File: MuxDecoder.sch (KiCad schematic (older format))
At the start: 2 parts, among them U3 4001, U4 4071

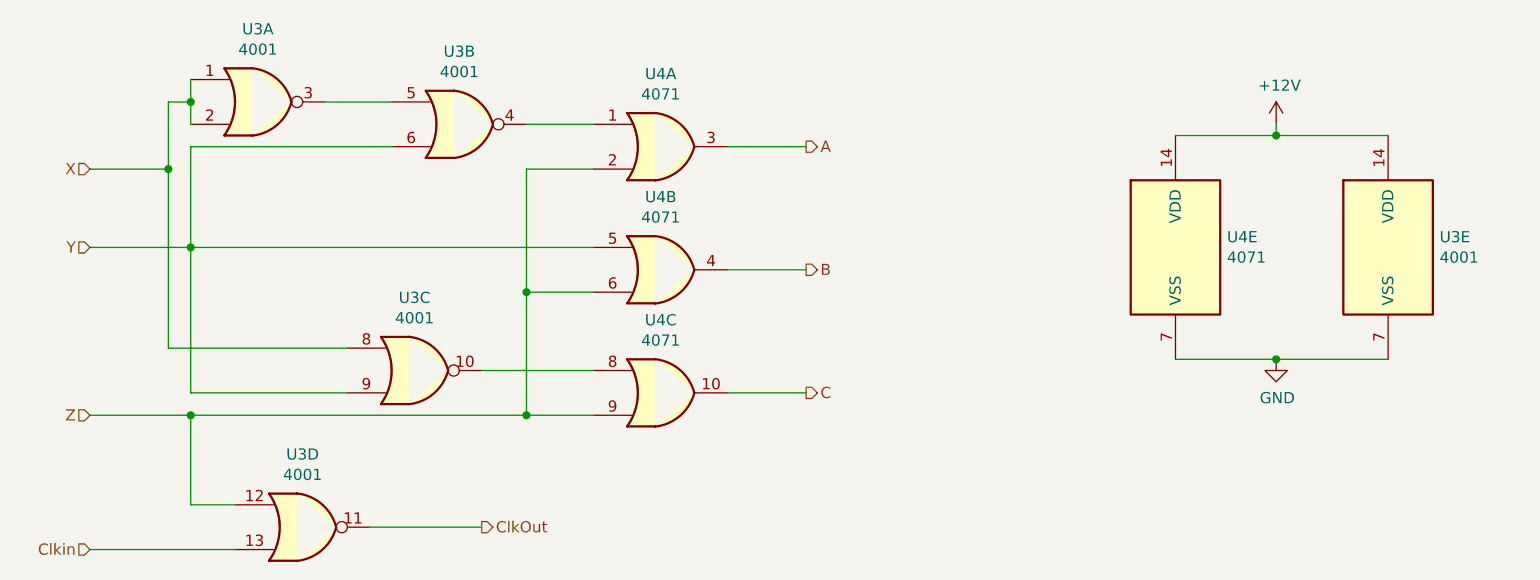
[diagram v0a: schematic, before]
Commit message: Renamed: NTE4001
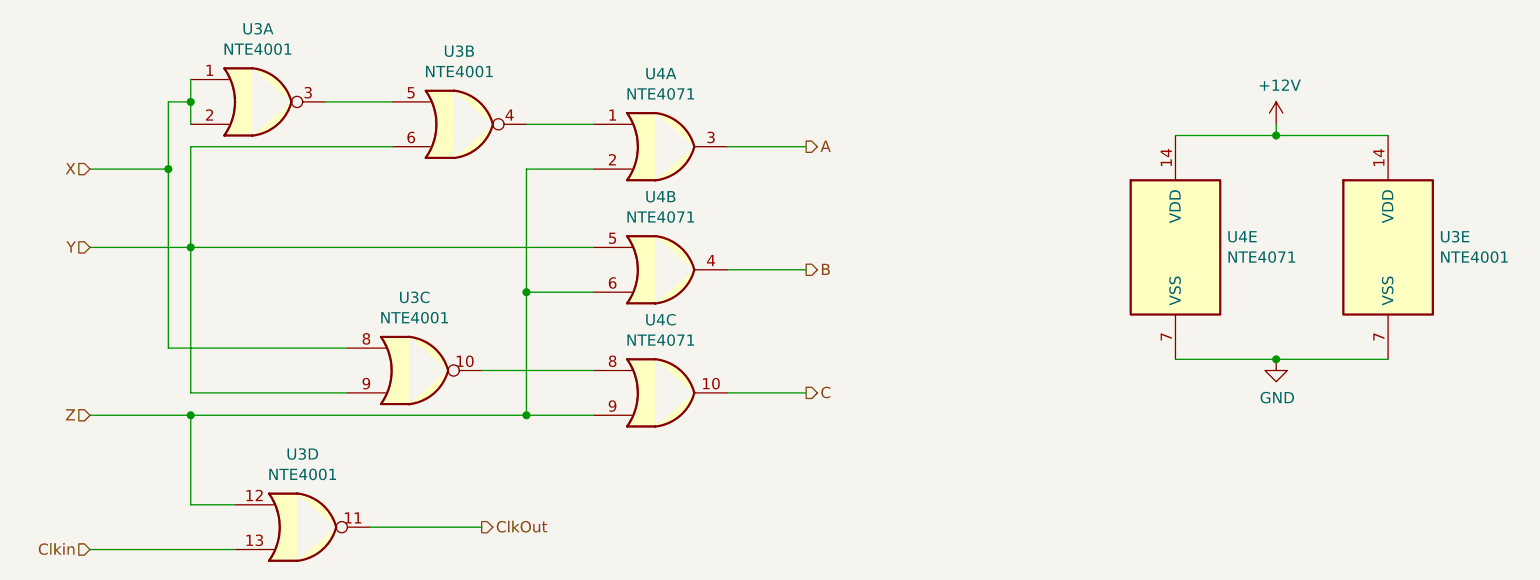
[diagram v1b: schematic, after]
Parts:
- U3: value 4001 -> NTE4001
- U4: value 4071 -> NTE4071
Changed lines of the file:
@@
 P 4650 1650
 F 0 "U4" H 4650 1975 50  0000 C CNN
-F 1 "4071" H 4650 1884 50  0000 C CNN
+F 1 "NTE4071" H 4650 1884 50  0000 C CNN
 F 2 "" H 4650 1650 50  0001 C CNN
 F 3 "http://www.intersil.com/content/dam/Intersil/documents/cd40/cd4071bms-72bms-75bms.pdf" H 4650 1650 50  0001 C CNN
@@
 P 4650 2200
 F 0 "U4" H 4650 2525 50  0000 C CNN
-F 1 "4071" H 4650 2434 50  0000 C CNN
+F 1 "NTE4071" H 4650 2434 50  0000 C CNN
 F 2 "" H 4650 2200 50  0001 C CNN
 F 3 "http://www.intersil.com/content/dam/Intersil/documents/cd40/cd4071bms-72bms-75bms.pdf" H 4650 2200 50  0001 C CNN
@@
 P 4650 2750
 F 0 "U4" H 4650 3075 50  0000 C CNN
-F 1 "4071" H 4650 2984 50  0000 C CNN
+F 1 "NTE4071" H 4650 2984 50  0000 C CNN
 F 2 "" H 4650 2750 50  0001 C CNN
 F 3 "http://www.intersil.com/content/dam/Intersil/documents/cd40/cd4071bms-72bms-75bms.pdf" H 4650 2750 50  0001 C CNN
@@
 P 6950 2100
 F 0 "U4" H 7180 2146 50  0000 L CNN
-F 1 "4071" H 7180 2055 50  0000 L CNN
+F 1 "NTE4071" H 7180 2055 50  0000 L CNN
 F 2 "" H 6950 2100 50  0001 C CNN
 F 3 "http://www.intersil.com/content/dam/Intersil/documents/cd40/cd4071bms-72bms-75bms.pdf" H 6950 2100 50  0001 C CNN
@@
 P 3750 1550
 F 0 "U3" H 3750 1875 50  0000 C CNN
-F 1 "4001" H 3750 1784 50  0000 C CNN
+F 1 "NTE4001" H 3750 1784 50  0000 C CNN
 F 2 "" H 3750 1550 50  0001 C CNN
 F 3 "http://www.intersil.com/content/dam/Intersil/documents/cd40/cd4000bms-01bms-02bms-25bms.pdf" H 3750 1550 50  0001 C CNN
@@
 P 3550 2650
 F 0 "U3" H 3550 2975 50  0000 C CNN
-F 1 "4001" H 3550 2884 50  0000 C CNN
+F 1 "NTE4001" H 3550 2884 50  0000 C CNN
 F 2 "" H 3550 2650 50  0001 C CNN
 F 3 "http://www.intersil.com/content/dam/Intersil/documents/cd40/cd4000bms-01bms-02bms-25bms.pdf" H 3550 2650 50  0001 C CNN
@@
 P 3050 3350
 F 0 "U3" H 3050 3675 50  0000 C CNN
-F 1 "4001" H 3050 3584 50  0000 C CNN
+F 1 "NTE4001" H 3050 3584 50  0000 C CNN
 F 2 "" H 3050 3350 50  0001 C CNN
 F 3 "http://www.intersil.com/content/dam/Intersil/documents/cd40/cd4000bms-01bms-02bms-25bms.pdf" H 3050 3350 50  0001 C CNN
@@
 P 7900 2100
 F 0 "U3" H 8130 2146 50  0000 L CNN
-F 1 "4001" H 8130 2055 50  0000 L CNN
+F 1 "NTE4001" H 8130 2055 50  0000 L CNN
 F 2 "" H 7900 2100 50  0001 C CNN
 F 3 "http://www.intersil.com/content/dam/Intersil/documents/cd40/cd4000bms-01bms-02bms-25bms.pdf" H 7900 2100 50  0001 C CNN
@@
 P 2850 1450
 F 0 "U3" H 2850 1775 50  0000 C CNN
-F 1 "4001" H 2850 1684 50  0000 C CNN
+F 1 "NTE4001" H 2850 1684 50  0000 C CNN
 F 2 "" H 2850 1450 50  0001 C CNN
 F 3 "http://www.intersil.com/content/dam/Intersil/documents/cd40/cd4000bms-01bms-02bms-25bms.pdf" H 2850 1450 50  0001 C CNN

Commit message: Added: pcb
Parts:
- U3, U4: footprint (none) -> Package_DIP:DIP-14_W7.62mm
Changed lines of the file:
@@
 F 0 "U4" H 4650 1975 50  0000 C CNN
 F 1 "NTE4071" H 4650 1884 50  0000 C CNN
-F 2 "" H 4650 1650 50  0001 C CNN
+F 2 "Package_DIP:DIP-14_W7.62mm" H 4650 1650 50  0001 C CNN
 F 3 "http://www.intersil.com/content/dam/Intersil/documents/cd40/cd4071bms-72bms-75bms.pdf" H 4650 1650 50  0001 C CNN
 	1    4650 1650
@@
 F 0 "U4" H 4650 2525 50  0000 C CNN
 F 1 "NTE4071" H 4650 2434 50  0000 C CNN
-F 2 "" H 4650 2200 50  0001 C CNN
+F 2 "Package_DIP:DIP-14_W7.62mm" H 4650 2200 50  0001 C CNN
 F 3 "http://www.intersil.com/content/dam/Intersil/documents/cd40/cd4071bms-72bms-75bms.pdf" H 4650 2200 50  0001 C CNN
 	2    4650 2200
@@
 F 0 "U4" H 4650 3075 50  0000 C CNN
 F 1 "NTE4071" H 4650 2984 50  0000 C CNN
-F 2 "" H 4650 2750 50  0001 C CNN
+F 2 "Package_DIP:DIP-14_W7.62mm" H 4650 2750 50  0001 C CNN
 F 3 "http://www.intersil.com/content/dam/Intersil/documents/cd40/cd4071bms-72bms-75bms.pdf" H 4650 2750 50  0001 C CNN
 	3    4650 2750
@@
 F 0 "U4" H 7180 2146 50  0000 L CNN
 F 1 "NTE4071" H 7180 2055 50  0000 L CNN
-F 2 "" H 6950 2100 50  0001 C CNN
+F 2 "Package_DIP:DIP-14_W7.62mm" H 6950 2100 50  0001 C CNN
 F 3 "http://www.intersil.com/content/dam/Intersil/documents/cd40/cd4071bms-72bms-75bms.pdf" H 6950 2100 50  0001 C CNN
 	5    6950 2100
@@
 F 0 "U3" H 3750 1875 50  0000 C CNN
 F 1 "NTE4001" H 3750 1784 50  0000 C CNN
-F 2 "" H 3750 1550 50  0001 C CNN
+F 2 "Package_DIP:DIP-14_W7.62mm" H 3750 1550 50  0001 C CNN
 F 3 "http://www.intersil.com/content/dam/Intersil/documents/cd40/cd4000bms-01bms-02bms-25bms.pdf" H 3750 1550 50  0001 C CNN
 	2    3750 1550
@@
 F 0 "U3" H 3550 2975 50  0000 C CNN
 F 1 "NTE4001" H 3550 2884 50  0000 C CNN
-F 2 "" H 3550 2650 50  0001 C CNN
+F 2 "Package_DIP:DIP-14_W7.62mm" H 3550 2650 50  0001 C CNN
 F 3 "http://www.intersil.com/content/dam/Intersil/documents/cd40/cd4000bms-01bms-02bms-25bms.pdf" H 3550 2650 50  0001 C CNN
 	3    3550 2650
@@
 F 0 "U3" H 3050 3675 50  0000 C CNN
 F 1 "NTE4001" H 3050 3584 50  0000 C CNN
-F 2 "" H 3050 3350 50  0001 C CNN
+F 2 "Package_DIP:DIP-14_W7.62mm" H 3050 3350 50  0001 C CNN
 F 3 "http://www.intersil.com/content/dam/Intersil/documents/cd40/cd4000bms-01bms-02bms-25bms.pdf" H 3050 3350 50  0001 C CNN
 	4    3050 3350
@@
 F 0 "U3" H 8130 2146 50  0000 L CNN
 F 1 "NTE4001" H 8130 2055 50  0000 L CNN
-F 2 "" H 7900 2100 50  0001 C CNN
+F 2 "Package_DIP:DIP-14_W7.62mm" H 7900 2100 50  0001 C CNN
 F 3 "http://www.intersil.com/content/dam/Intersil/documents/cd40/cd4000bms-01bms-02bms-25bms.pdf" H 7900 2100 50  0001 C CNN
 	5    7900 2100
@@
 F 0 "U3" H 2850 1775 50  0000 C CNN
 F 1 "NTE4001" H 2850 1684 50  0000 C CNN
-F 2 "" H 2850 1450 50  0001 C CNN
+F 2 "Package_DIP:DIP-14_W7.62mm" H 2850 1450 50  0001 C CNN
 F 3 "http://www.intersil.com/content/dam/Intersil/documents/cd40/cd4000bms-01bms-02bms-25bms.pdf" H 2850 1450 50  0001 C CNN
 	1    2850 1450
